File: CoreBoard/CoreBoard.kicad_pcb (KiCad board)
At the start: 2 copper layers, 144.8 x 89.5 mm, 84 parts, among them J1 RJ45_LED_Shielded, SW1 SW_Push, SW10 SW_Push, SW11 SW_Wuerth_450301014042, SW12 SW_Wuerth_450301014042, SW13 SW_Wuerth_450301014042, SW14 SW_Wuerth_450301014042, SW15 SW_Wuerth_450301014042, SW16 SW_Wuerth_450301014042, SW17 SW_Wuerth_450301014042, SW2 SW_Push, SW3 SW_Push, SW4 SW_Push, SW5 SW_Push, SW6 SW_Push, SW7 SW_Push, SW8 SW_Push, SW9 SW_Push, U1 OKI, U2 Teensy4.1_DEV-16771, U3 SHHD003A0A, U4 GY-521, U5 ATA6561, U6 74HC148, U7 74HC148, U8 74HC00

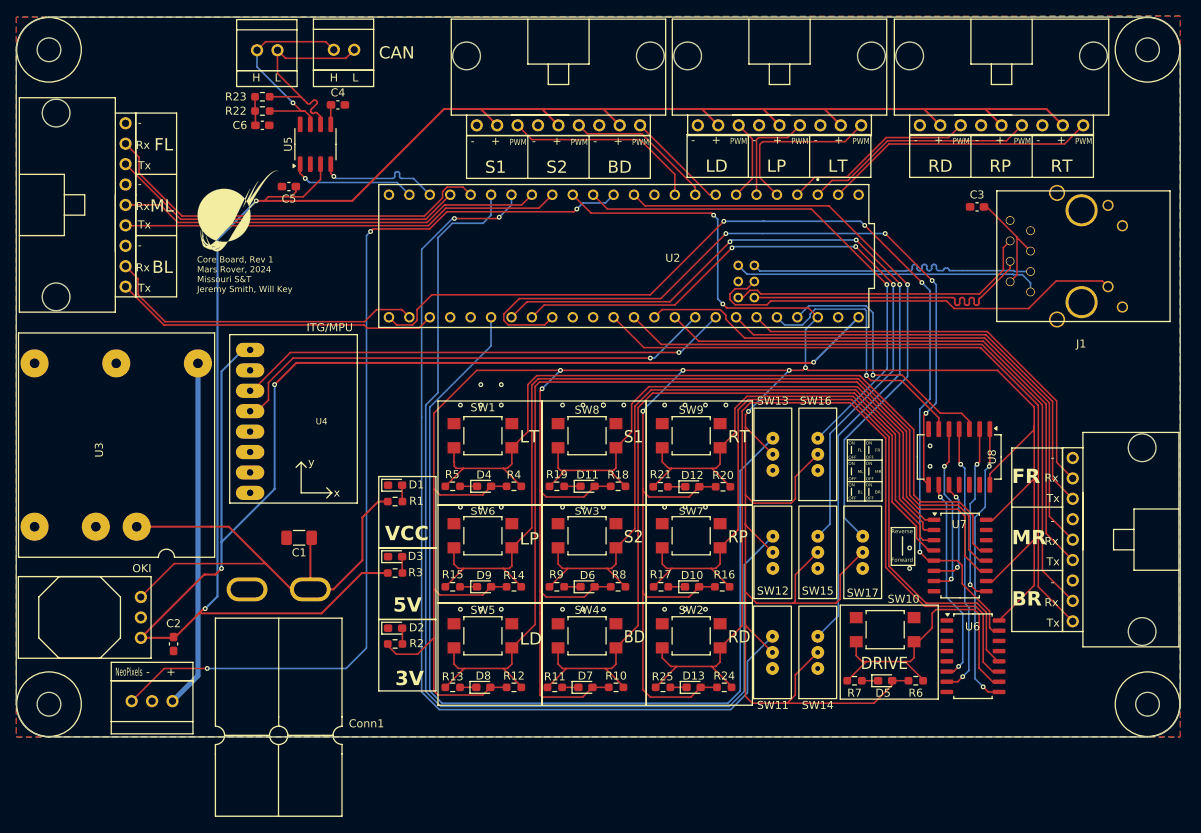
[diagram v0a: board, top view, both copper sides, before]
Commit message: Shifted ethernet port and traces down the board as to not interfere with the Teensy USB port, and changed the layers on which several traces run to free up the ground plane near the ground anderson
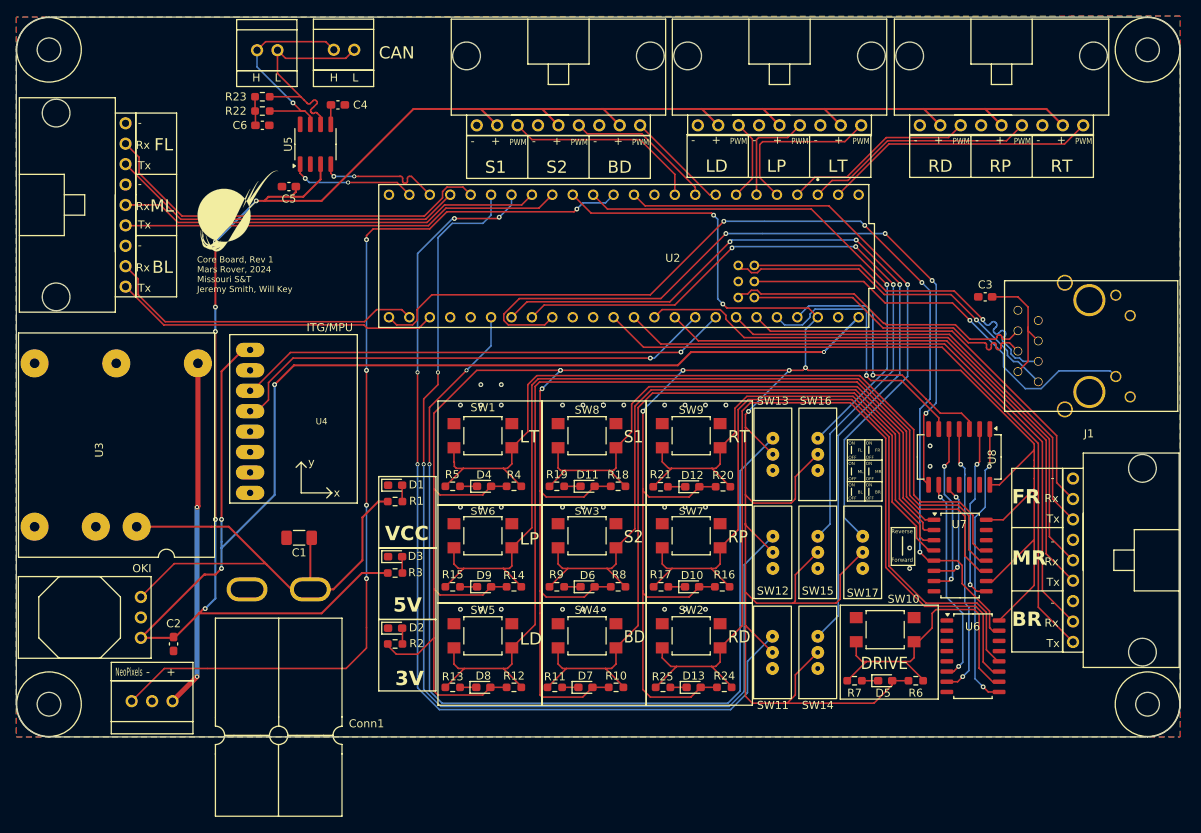
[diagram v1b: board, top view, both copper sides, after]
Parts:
- moved C3 11.2 mm to (172.0, 72.9)
- moved J1 11.2 mm to (197.9, 78.9)
- moved Conn4 2.56 mm to (182.9, 95.5)
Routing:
- net Tx+: track 38.4 -> 44.0 mm, vias 0 -> 1
- net +3.3V: track 523.6 -> 518.0 mm
- net Tx-: track 38.2 -> 43.6 mm, vias 0 -> 1
- net Net-(C3-Pad1): track 14.0 -> 15.8 mm
- net LED: track 54.0 -> 52.6 mm, vias 0 -> 1
- net +5V: track 370.8 -> 371.6 mm, vias 5 -> 10
- net Rx+: track 38.6 -> 38.0 mm
- net DS1: track 120.4 -> 120.8 mm, vias 2 -> 4
- net DS2: track 129.3 -> 129.5 mm, vias 0 -> 2
- net CAN_RX: vias 1 -> 2
- net DS3: track 122.6 -> 122.7 mm, vias 0 -> 2
- net NeoPixels: vias 3 -> 5
- net /5V: vias 0 -> 2
- net CAN_TX: vias 1 -> 2

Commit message: Fixed silkscreens problems raised in CDR; switch labels and power label
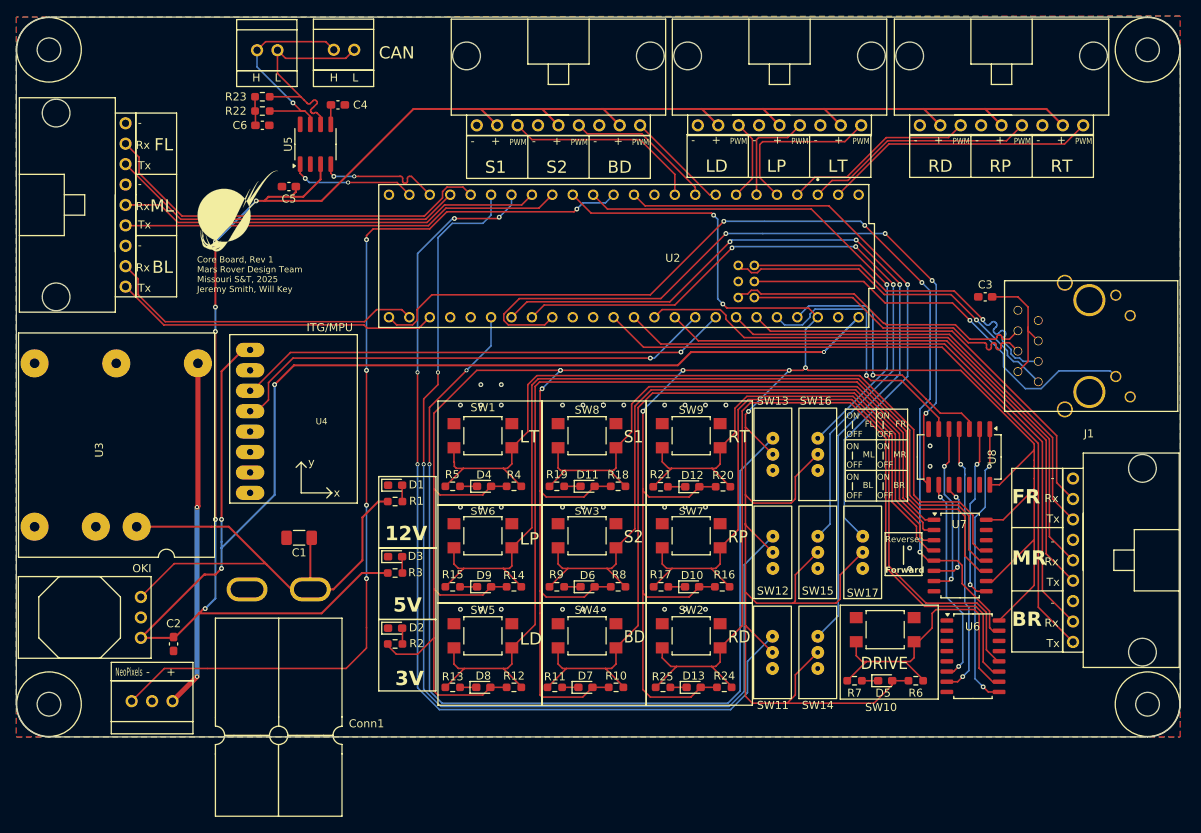
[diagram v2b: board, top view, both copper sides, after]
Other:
- board text added: "12V"
- board text added: "Core Board, Rev 1 Mars Rover Design Team Missouri S&T, 2025 Jeremy Smith, Will Key"
- board text removed: "Core Board, Rev 1 Mars Rover, 2024 Missouri S&T Jeremy Smith, Will Key"
- board text removed: "VCC"

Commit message: Added vias to get rid of ground voids and added a mounting hole as a standoff for the accelerometer
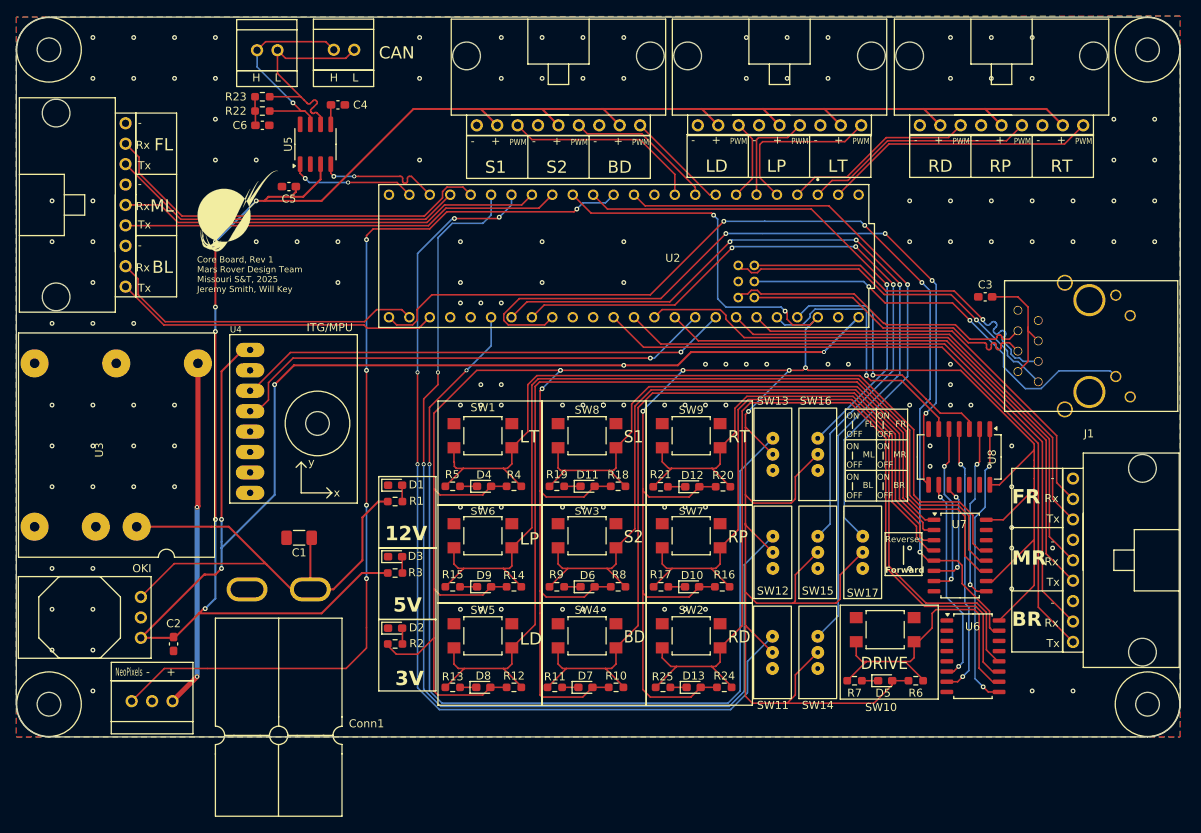
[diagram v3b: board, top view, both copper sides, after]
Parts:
- added H4: MountingHole, MRDT_Drill_Holes:4_40_Hole, F.Cu at (88.9, 88.6)
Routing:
- net +3.3V: track 518.0 -> 519.3 mm
- net LED: vias 1 -> 2
- net GND: vias 36 -> 147
- net +5V: vias 10 -> 11

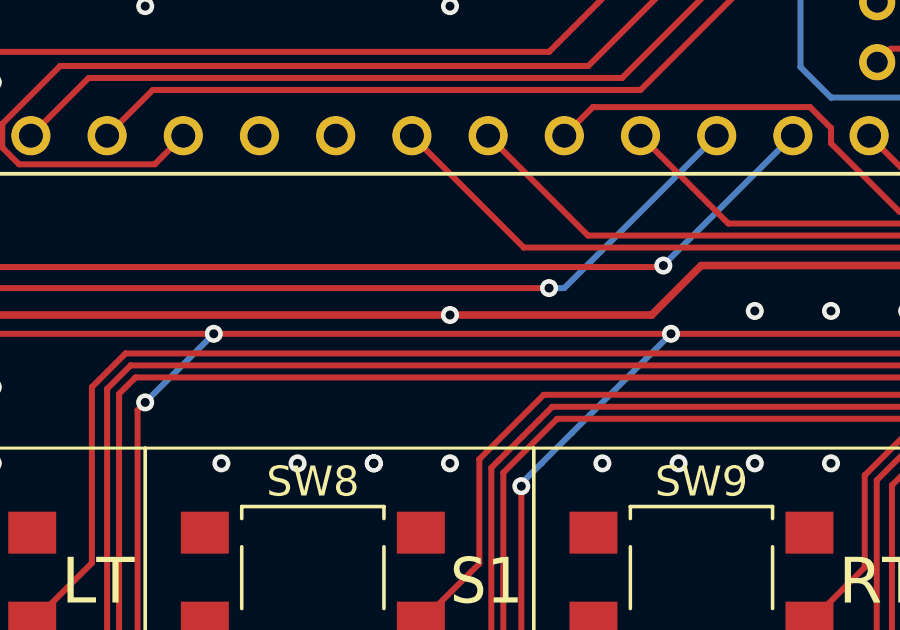
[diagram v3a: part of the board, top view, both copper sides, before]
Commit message: Removed extra 5V via
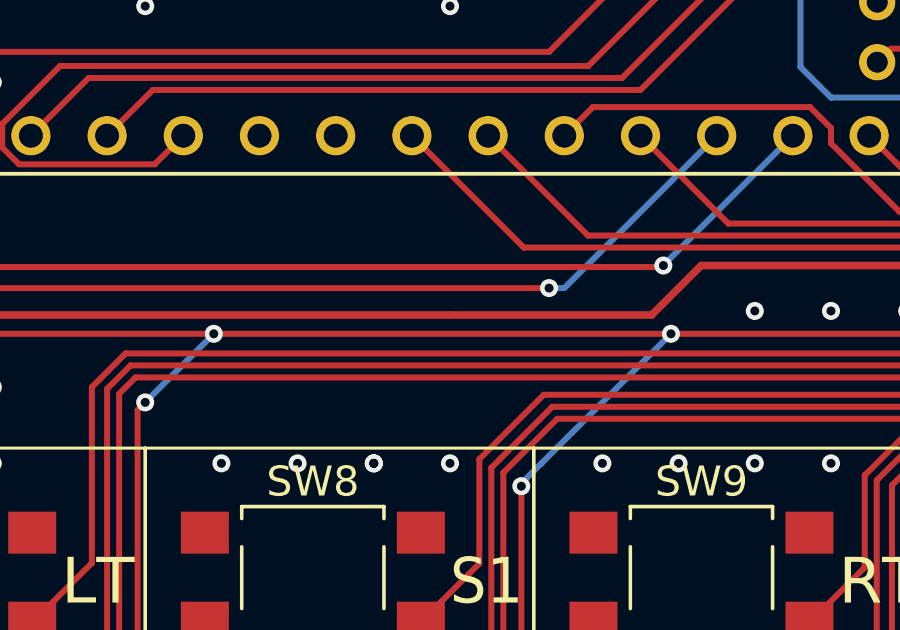
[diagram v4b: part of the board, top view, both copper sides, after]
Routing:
- net +5V: vias 11 -> 10
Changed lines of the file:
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@@
-	)
-	(via
-		(at 127 81.415)
-		(size 0.6)
-		(drill 0.3)
-		(layers "F.Cu" "B.Cu")
-		(net 3)
 	)
 	(via

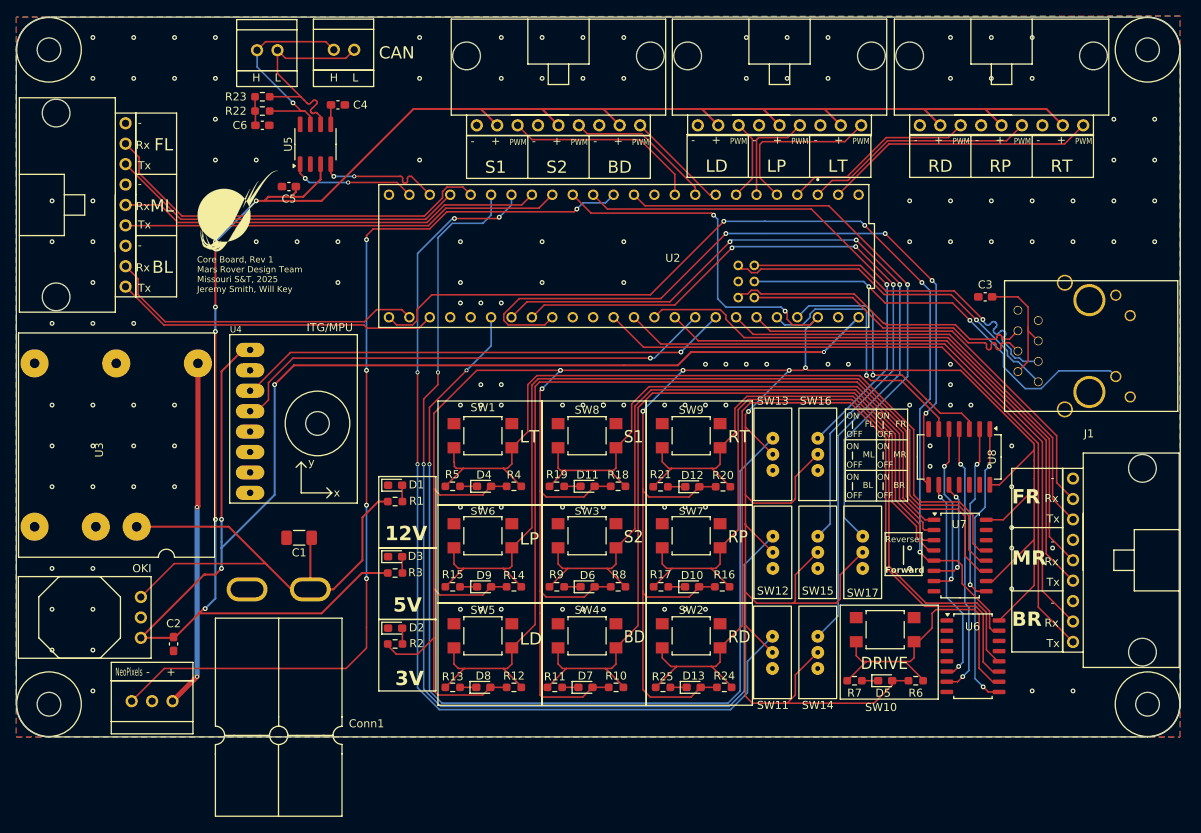
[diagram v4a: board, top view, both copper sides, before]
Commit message: Created Manufacturing files, adjusted mounting holes, and added standoff holes for accelerometer
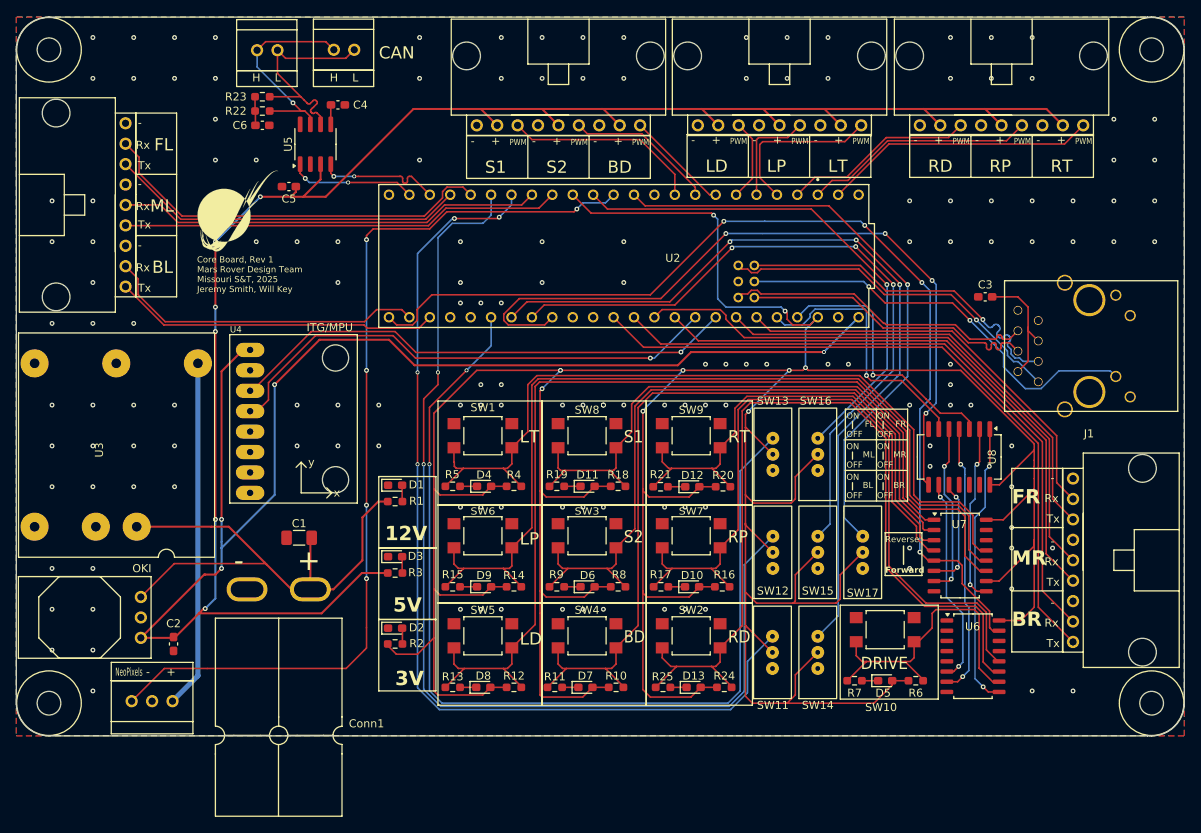
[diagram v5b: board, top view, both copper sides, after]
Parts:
- removed the H4 at (88.9, 88.6)
- moved H3 0.52 mm to (192.7, 123.4)
- moved H2 0.51 mm to (192.7, 42.2)
- moved H4 0.13 mm to (55.5, 123.4)
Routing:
- net +5V: track 371.6 -> 369.2 mm
- net AccSDA: track 61.5 -> 63.8 mm
- net AccSCL: track 61.7 -> 63.9 mm
- net +3.3V: track 519.3 -> 521.3 mm
- net /5V: vias 2 -> 0
- net GND: vias 147 -> 153
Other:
- board size 144.8 x 89.5 mm -> 145.3 x 89.4 mm
